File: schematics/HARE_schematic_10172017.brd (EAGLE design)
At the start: 105.1 x 80 mm, 14 parts, among them IC1 NE5532N, IC2 NE5532N, IC3 FT232RL, J2 STEREOSWL, J3 STEREOSWL, SW1 3PDTBLUE, U1 ATMEGA328P-PU, X2 USB-B-H

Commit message: Updated schematic and board layout
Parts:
- added C1, C10, C13, C14, C15, C16, C17, C18, C2, C8, C9: 1uF, resistor:C0805K
- added C11, C12: 0.22uF, resistor:C0805K
- added C3: 10uF, resistor:C0805K
- added C4, C5, C6, C7: 0.01uF, resistor:C0805K
- added D1, D3, D4, D5: LED5MM, gm-diodes:LED5MM
- added D2: 1N4148-3, gm-diodes:DO35-3
- added IC4: NE5532N, gm-ics:DIL08
- added LDR1, LDR2, LDR3: (no value), gm-resistors:LDR338-54C
- added R1: 470, rcl:M0805
- added R10, R11, R16, R18, R19, R2, R20, R21, R22, R23, R3, R4, R7, R8: 1k, resistor:R0805
- added R12, R9: 2.2k, resistor:R0805
- added R13: 47k, resistor:R0805
- added R14: 100k, resistor:R0805
- added R15, R17: 10k, resistor:R0805
- added R24, R25: 10k, resistor:RTRIM3314G
- added R5, R6: 10k, rcl:M0805
- moved IC3 8.89 mm to (7.62, 58.4)
- moved IC2 1.80 mm to (94.0, 45.7)
- moved IC1 1.27 mm to (94.0, 30.5)
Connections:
- removed net V+: IC1.8, IC2.8
- removed net V-: IC1.4, IC2.4
- new net 5V: LDR1.2
- new net ADC_IN: R21.2
- new net BYPASS: SW1.A3, SW1.C3
- new net DAC_OUT: C8.2
- new net DRY: R22.2
- new net INPUT: J2.T, SW1.A2, SW1.B3
- new net N$10: C1.2, R2.2
- new net N$11: IC4.2, R2.1, R3.2
- new net N$12: C4.2, R7.2, R8.1, R9.1
- new net N$13: C5.2, IC1.2, R8.2
- new net N$14: C5.1, IC1.1, R10.1, R9.2
- new net N$15: C8.1, R7.1
- new net N$16: C7.2, R10.2, R11.1, R12.1
- new net N$17: C6.2, IC1.6, R11.2
- new net N$18: C6.1, C9.2, IC1.7, R12.2
- new net N$19: J3.T, SW1.C1
- new net N$21: C10.1, R13.1
- new net N$22: C11.2, IC2.2, R13.2, R14.1
- new net N$23: C13.2, IC2.1, LDR2.2, R14.2, R15.2
- new net N$24: IC2.3
- new net N$25: C12.1, LDR2.1, R15.1
- new net N$26: C10.2
- new net N$27: C11.1, C12.2, D2.A, R16.2
- new net N$28: IC2.5
- new net N$29: LDR1.1, R16.1, R17.2
- new net N$30: C14.1, R18.1
- new net N$31: C15.2, LDR3.2, R18.2
- new net N$32: C15.1, R19.1
- new net N$33: IC2.6, R19.2, R20.1
- new net N$34: C16.2, IC2.7, R20.2
- new net N$35: C14.2
- new net N$36: C2.2, R21.1, R22.1
- new net N$37: C2.1, IC4.1, R25.1
- new net N$38: IC4.3
- new net N$39: C17.2
- new net N$40: C17.1, R4.1
- new net N$41: IC4.6, R23.1, R4.2
- new net N$42: R23.2, R24.2, R24.3
- new net N$43: C18.2, IC4.7, R24.1
- new net N$44: IC4.5
- new net N$45: APOT2.3, C18.1
- new net N$46: APOT1.3, APOT2.2
- new net N$47: APOT1.2, SW1.C2
- new net N$48: APOT1.1
- new net N$49: R25.2, R25.3, R3.1
- new net N$7: D1.A, R1.2
- new net N$8: D1.K, SW1.B1
- new net N$9: C1.1, SW1.A1
- new net VCA_IN: C13.1
- new net VCA_OUT: C16.1
- new net VCF_IN: C9.1
- new net V_BIAS: C3.2, IC1.3, IC1.5, R5.2, R6.1
- net GND: now also APOT2.1, C3.1, C4.1, C7.1, D2.C, IC1.4, IC2.4, IC4.4, J1.3, J2.G, J2.R, J2.RN, J2.S, J3.G, J3.R, J3.RN, J3.S, LDR3.1, R17.1, R6.2, SW1.B2
- net VCC: now also IC1.8, IC2.8, IC4.8, J1.1, J1.2, R1.1, R5.1

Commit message: Updating first schematic build
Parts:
- added C19, C25: 10uF, resistor:C0805K
- added C20, C21: 22pF, resistor:C0805K
- added C22, C23, C24: 0.1uF, resistor:C0805K
- added IC5: 7805DT, gm-regulators:TO252
- added Q1: 16 MHz, special:QS
- added R26, R27, R28: 1k, resistor:R0805
- added R29: 10k, resistor:R0805
- J2, J3: value STEREOSWL -> STEREOSW; device gm-jacks:NRJ6HF-1 -> gm-jacks:NMJ6HCD2
- moved R8 47.1 mm to (53.3, 24.1)
- moved LDR2 45.8 mm to (36.8, 54.6), turned to 0 degrees
- moved C4 41.3 mm to (47.0, 27.9)
- moved R22 27.7 mm to (58.4, 43.2), turned to 90 degrees
- moved D2 23.3 mm to (63.5, 39.4), turned to 90 degrees
- moved C9 22.2 mm to (64.8, 16.5), turned to 90 degrees
- moved IC3 21.6 mm to (7.62, 36.8)
- moved C7 19.7 mm to (64.8, 22.9)
- moved C8 19.1 mm to (64.8, 10.2), turned to 270 degrees
- moved C1 14.2 mm to (34.3, 7.62), turned to 90 degrees
- moved R12 13.3 mm to (71.1, 20.3), turned to 270 degrees
- moved D5 11.7 mm to (30.5, 54.6), turned to 270 degrees
- moved C16 11.4 mm to (29.2, 20.3), turned to 90 degrees
- moved C2 11.4 mm to (29.2, 7.62), turned to 90 degrees
- moved R7 9.92 mm to (59.7, 24.1)
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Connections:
- removed net AVCC: U1.20
- new net ADC1: DPOT1.2, U1.24
- new net ADC2: DPOT2.2, U1.25
- new net ADC3: DPOT3.2, U1.26
- new net N$50: IC3.1
- new net N$51: C21.2, Q1.1, U1.10
- new net N$52: IC3.15, X2.D+
- new net N$53: IC3.16, X2.D-
- new net N$54: C24.2, IC3.17
- new net N$55: IC3.5
- new net N$56: R28.2, U1.12
- new net N$57: D5.A, R28.1
- new net N$58: R27.2, U1.11
- new net N$59: D4.A, R27.1
- new net N$60: R26.2, U1.5
- new net N$61: D3.A, R26.1
- new net N$62: IC3.19, R29.2
- new net OSC: C20.2, Q1.2, U1.9
- new net RXD: U1.2
- new net TXD: U1.3
- net 5V: now also C19.2, C22.2, C23.2, DPOT1.3, DPOT2.3, DPOT3.3, IC3.20, IC5.2, R29.1, U1.20, U1.7, X2.VBUS
- net ADC_IN: now also U1.23
- net GND: now also C19.1, C20.1, C21.1, C22.1, C23.1, C24.1, C25.1, D3.K, D4.K, D5.K, DPOT1.1, DPOT2.1, DPOT3.1, IC3.26, IC5.3, J2.SN, J3.SN, U1.8, X2.GND; no longer J2.G, J3.G
- net INPUT: now also J2.TN
- net N$19: now also J3.TN
- net VCC: now also C25.2, IC5.1; no longer IC3.20, U1.7

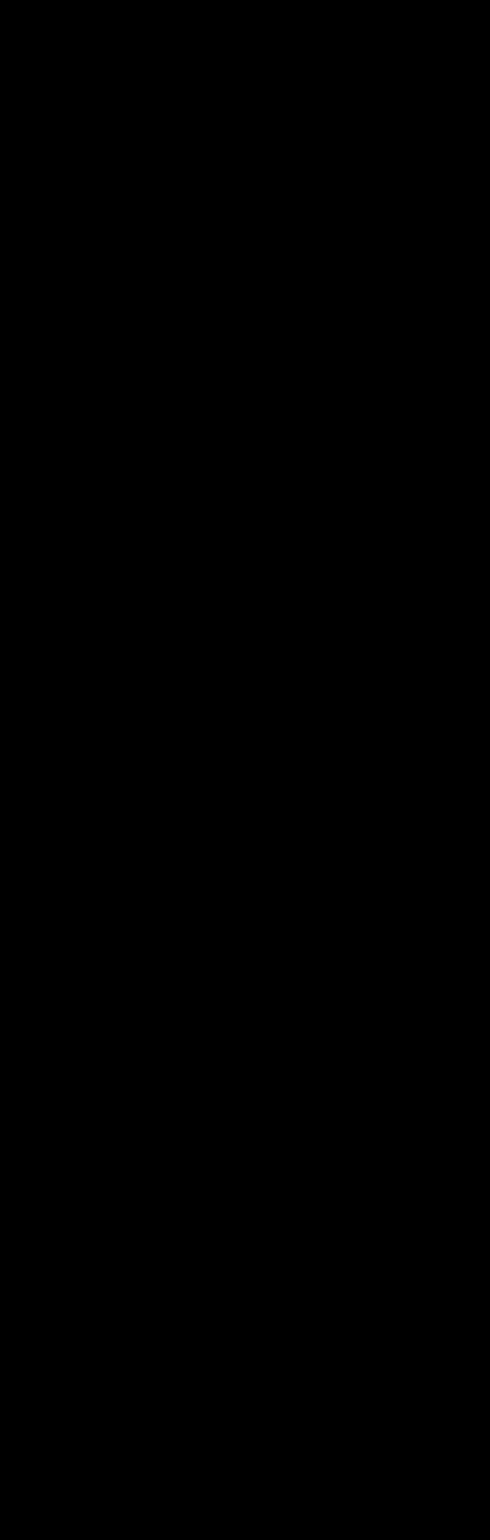
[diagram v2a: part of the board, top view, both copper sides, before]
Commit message: Update board layout
Update board layout to match schematic updates.
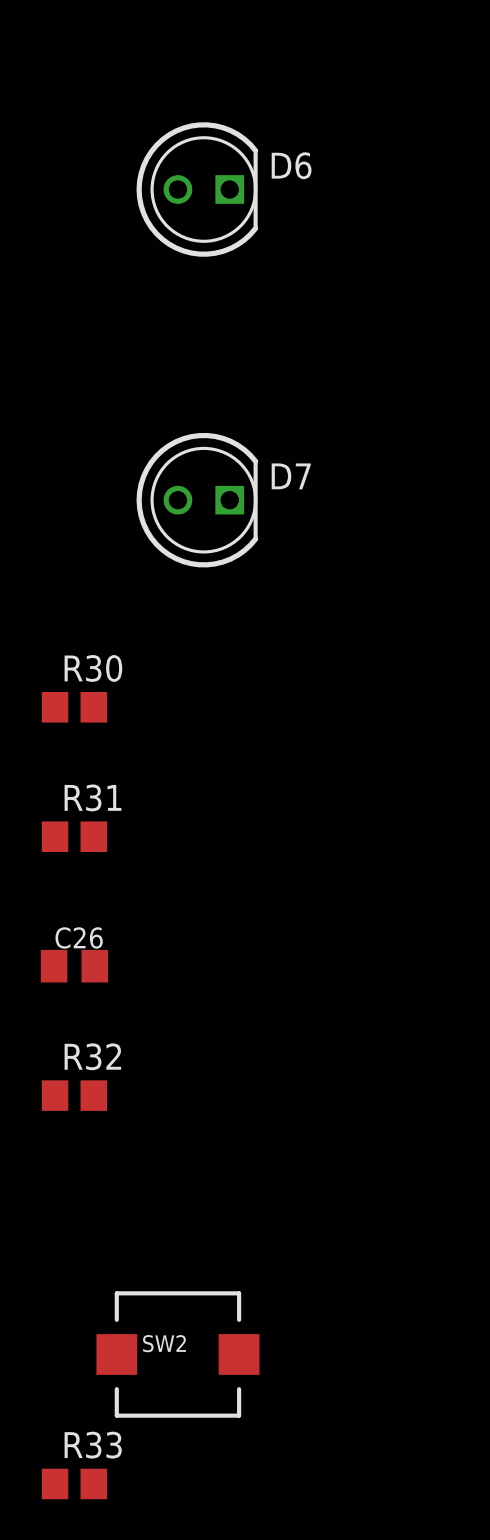
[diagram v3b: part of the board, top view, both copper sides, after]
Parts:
- added C26: 100nF, resistor:C0805K
- added D6, D7: LED5MM, gm-diodes:LED5MM
- added R30, R31, R32: 1k, resistor:R0805
- added R33: 10k, resistor:R0805
- added SW2: Reset Button, adafruit:PUSHBUTTON_SMD_SJ
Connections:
- removed net N$50: IC3.1
- removed net N$55: IC3.5
- new net CBUS1: D6.K
- new net CBUS2: D7.K
- new net CTS#: IC3.11, U1.4
- new net N$63: D6.A, R30.2
- new net N$64: D7.A, R31.2
- new net N$65: IC3.13
- new net N$66: IC3.22
- new net N$68: IC3.4
- new net RESET#: R32.1, R33.2, SW2.P$2, U1.1
- new net RTS#: IC3.3, R32.2
- net 5V: now also C26.2, R33.1
- net GND: now also C26.1, SW2.P$1
- net RXD: now also IC3.5
- net TXD: now also IC3.1
- net VCCIO: now also R30.1, R31.1; no longer IC3.4
